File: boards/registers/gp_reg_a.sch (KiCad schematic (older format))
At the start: 19 parts, among them U28 MC74AC273DTR2G, U29 SN74ACT244PW

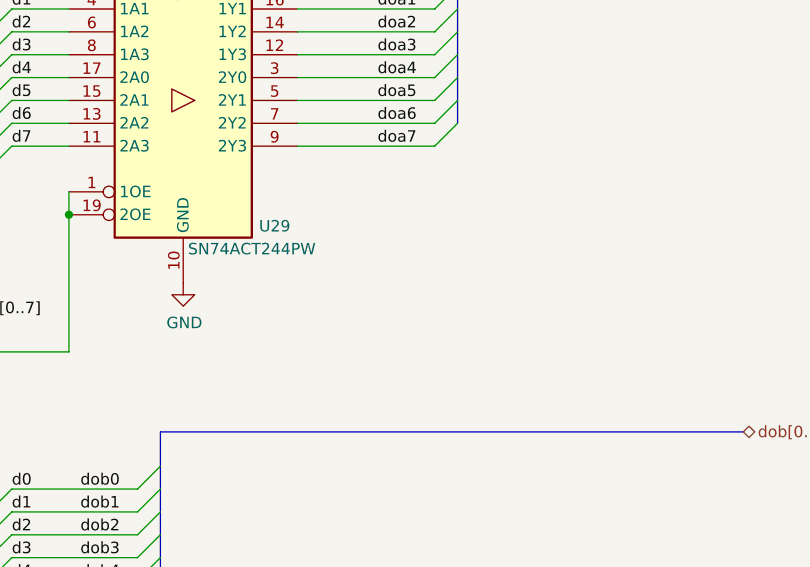
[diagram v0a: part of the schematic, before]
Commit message: Registers: more decoupling capacitors
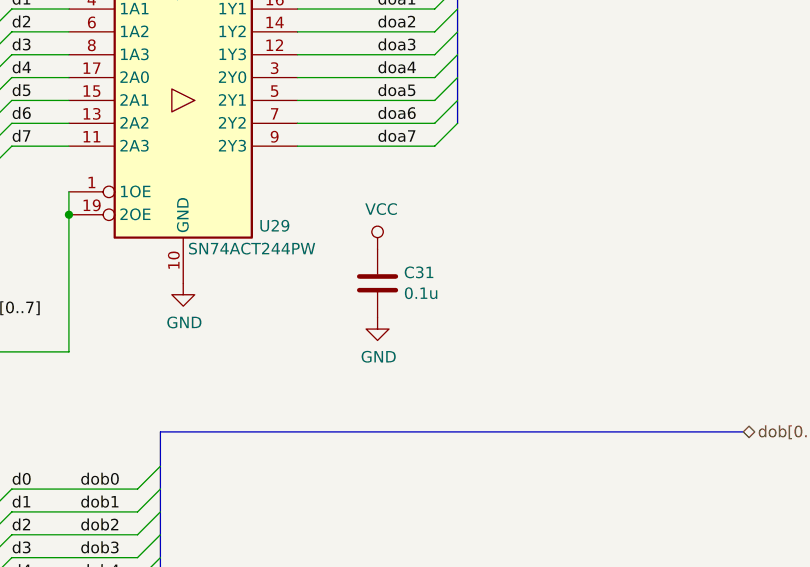
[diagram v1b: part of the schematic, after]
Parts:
- added C31: 0.1u, Capacitor_SMD:C_0805_2012Metric, symbol Device:C
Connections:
- net GND: now also C31.2
- net VCC: now also C31.1
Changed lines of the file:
@@
 Wire Wire Line
 	7750 1200 8350 1200
+$Comp
+L Device:C C?
+U 1 1 60132E7F
+P 8100 2500
+AR Path="/60132E7F" Ref="C?"  Part="1"
+AR Path="/5E9FD18D/60132E7F" Ref="C31"  Part="1"
+F 0 "C31" H 8215 2546 50  0000 L CNN
+F 1 "0.1u" H 8215 2455 50  0000 L CNN
+F 2 "Capacitor_SMD:C_0805_2012Metric" H 8138 2350 50  0001 C CNN
+F 3 "~" H 8100 2500 50  0001 C CNN
+	1    8100 2500
+	1    0    0    -1
+$EndComp
+$Comp
+L power:VCC #PWR?
+U 1 1 60132E85
+P 8100 2350
+AR Path="/60132E85" Ref="#PWR?"  Part="1"
+AR Path="/5E9FD18D/60132E85" Ref="#PWR0229"  Part="1"
+F 0 "#PWR0229" H 8100 2200 50  0001 C CNN
+F 1 "VCC" H 8117 2523 50  0000 C CNN
+F 2 "" H 8100 2350 50  0001 C CNN
+F 3 "" H 8100 2350 50  0001 C CNN
+	1    8100 2350
+	1    0    0    -1
+$EndComp
+$Comp
+L power:GND #PWR?
+U 1 1 60132E8B
+P 8100 2650
+AR Path="/60132E8B" Ref="#PWR?"  Part="1"
+AR Path="/5E9FD18D/60132E8B" Ref="#PWR0230"  Part="1"
+F 0 "#PWR0230" H 8100 2400 50  0001 C CNN
+F 1 "GND" H 8105 2477 50  0000 C CNN
+F 2 "" H 8100 2650 50  0001 C CNN
+F 3 "" H 8100 2650 50  0001 C CNN
+	1    8100 2650
+	1    0    0    -1
+$EndComp
 Wire Bus Line
 	7150 3150 7150 4000

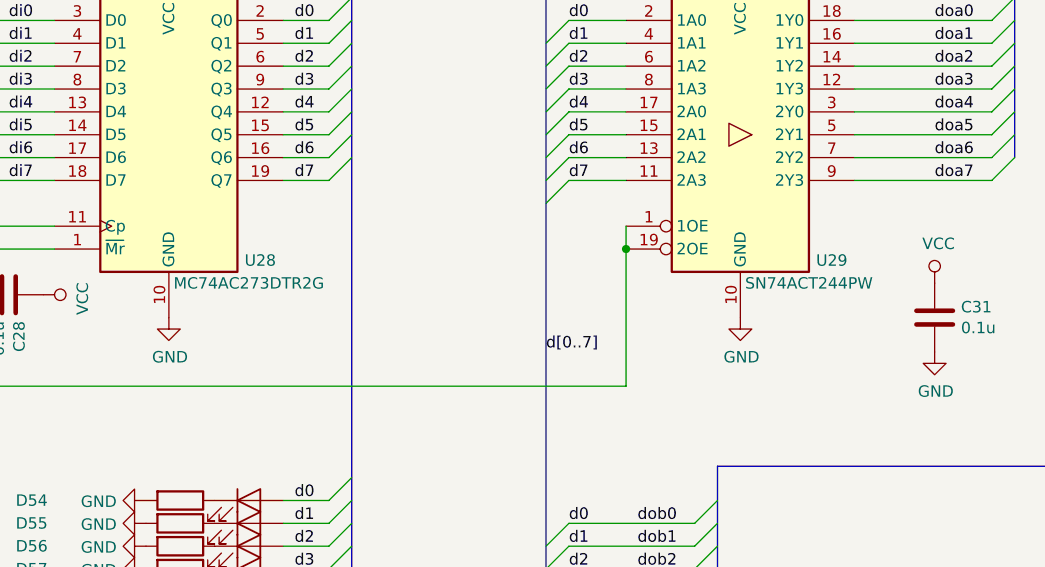
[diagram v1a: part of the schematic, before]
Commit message: Registers: change logic family to HC and LV-A
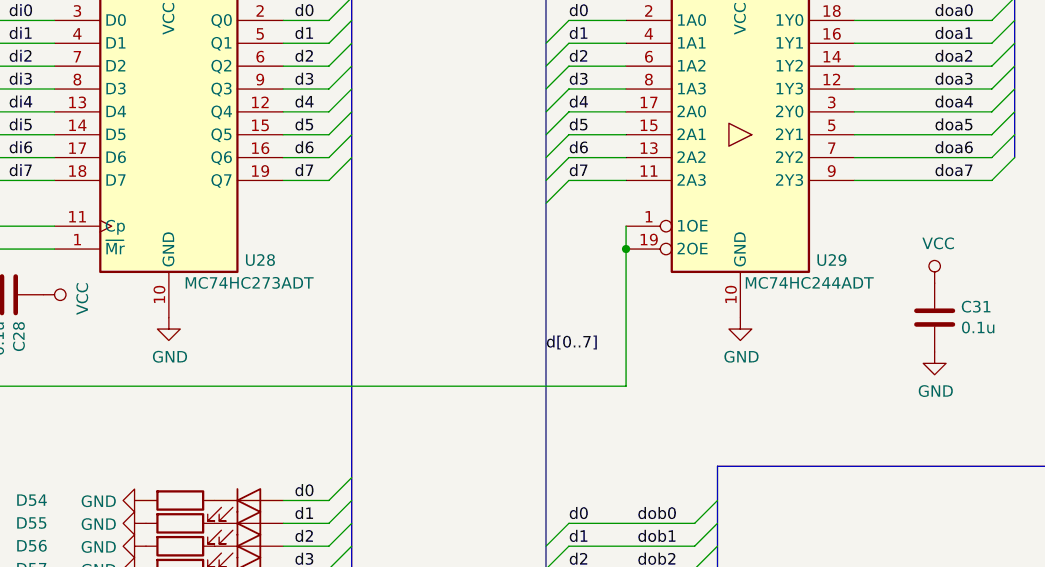
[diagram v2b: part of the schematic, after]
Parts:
- U28: value MC74AC273DTR2G -> MC74HC273ADT
- U29: value SN74ACT244PW -> MC74HC244ADT
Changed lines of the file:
@@
 AR Path="/5E9FD18D/5EA6BD49" Ref="U29"  Part="1"
 F 0 "U29" H 7650 1150 50  0000 C CNN
-F 1 "SN74ACT244PW" H 7550 1050 50  0000 C CNN
+F 1 "MC74HC244ADT" H 7550 1050 50  0000 C CNN
 F 2 "Package_SO:TSSOP-20_4.4x6.5mm_P0.65mm" H 7250 1700 50  0001 C CNN
-F 3 "https://assets.nexperia.com/documents/data-sheet/74HC_HCT244.pdf" H 7250 1700 50  0001 C CNN
+F 3 "http://www.farnell.com/datasheets/1878565.pdf" H 7250 1700 50  0001 C CNN
 	1    7250 1700
 	1    0    0    -1
@@
 AR Path="/5E9FD18D/5EA6BDD0" Ref="U28"  Part="1"
 F 0 "U28" H 5150 1150 50  0000 C CNN
-F 1 "MC74AC273DTR2G" H 5100 1050 50  0000 C CNN
+F 1 "MC74HC273ADT" H 5100 1050 50  0000 C CNN
 F 2 "Package_SO:TSSOP-20_4.4x6.5mm_P0.65mm" H 4750 1700 50  0001 C CNN
-F 3 "https://assets.nexperia.com/documents/data-sheet/74HC_HCT273.pdf" H 4750 1700 50  0001 C CNN
+F 3 "http://www.farnell.com/datasheets/1878567.pdf" H 4750 1700 50  0001 C CNN
 	1    4750 1700
 	1    0    0    -1
